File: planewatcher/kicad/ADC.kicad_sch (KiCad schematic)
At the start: 15 parts, among them U11 AD9203ARUZ

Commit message: update BoM to available parts from LCSC
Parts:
- RN2, RN3, RN4: MPN CAT16-22R0F4LF -> CAY16-22R0F4LF; lcsc_id C1731387 -> C1734385
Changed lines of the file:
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@@
 			)
 		)
-		(property "MPN" "CAT16-22R0F4LF"
+		(property "MPN" "CAY16-22R0F4LF"
 			(at 45.72 85.09 0)
 			(hide yes)
@@
 			)
 		)
-		(property "lcsc_id" "C1731387"
+		(property "lcsc_id" "C1734385"
 			(at 45.72 85.09 0)
 			(hide yes)
@@
 			)
 		)
-		(property "MPN" "CAT16-22R0F4LF"
+		(property "MPN" "CAY16-22R0F4LF"
 			(at 58.42 74.93 0)
 			(hide yes)
@@
 			)
 		)
-		(property "lcsc_id" "C1731387"
+		(property "lcsc_id" "C1734385"
 			(at 58.42 74.93 0)
 			(hide yes)
@@
 			)
 		)
-		(property "MPN" "CAT16-22R0F4LF"
+		(property "MPN" "CAY16-22R0F4LF"
 			(at 45.72 93.98 0)
 			(hide yes)
@@
 			)
 		)
-		(property "lcsc_id" "C1731387"
+		(property "lcsc_id" "C1734385"
 			(at 45.72 93.98 0)
 			(hide yes)

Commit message: Implement log detector output buffering & buffered low-pass filter for noise offset
- Implement low-pass filter to output noise floor with no pulses
- Feed noise floor into ADC driver -IN to improve range/sensitivity
- Buffer low pass filter output
- Buffer log detector output with spare op amp in OPA2320 package
- Tidy schematic & vias
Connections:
- net VREF: no longer names the net of C57.1, C58.1, TP21.1, U11.23 (VREF)
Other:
- moved on the sheet: TP21
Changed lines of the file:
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@@
+	)
+	(junction
+		(at 45.72 62.23)
+		(diameter 0)
+		(color 0 0 0 0)
 	)
 	(junction
@@
 	)
 	(junction
-		(at 45.72 62.23)
-		(diameter 0)
-		(color 0 0 0 0)
-	)
-	(junction
 		(at 59.69 62.23)
 		(diameter 0)
@@
 	)
 	(junction
-		(at 128.27 97.79)
-		(diameter 0)
-		(color 0 0 0 0)
-	)
-	(junction
 		(at 107.95 62.23)
 		(diameter 0)
@@
 		(pts
 			(xy 97.79 54.61) (xy 107.95 54.61)
-		)
-		(stroke
-			(width 0)
-			(type default)
-		)
-	)
-	(wire
-		(pts
-			(xy 128.27 97.79) (xy 135.89 97.79)
 		)
 		(stroke
@@
 	(wire
 		(pts
+			(xy 135.89 97.79) (xy 148.59 97.79)
+		)
+		(stroke
+			(width 0)
+			(type default)
+		)
+	)
+	(wire
+		(pts
 			(xy 64.77 90.17) (xy 69.85 90.17)
 		)
@@
 	(wire
 		(pts
-			(xy 121.92 97.79) (xy 128.27 97.79)
-		)
-		(stroke
-			(width 0)
-			(type default)
-		)
-	)
-	(wire
-		(pts
-			(xy 148.59 97.79) (xy 135.89 97.79)
+			(xy 121.92 97.79) (xy 135.89 97.79)
 		)
 		(stroke
@@
 		(shape input)
 		(at 97.79 66.04 0)
-		(effects
-			(font
-				(size 1.27 1.27)
-			)
-			(justify left)
-		)
-	)
-	(hierarchical_label "VREF"
-		(shape output)
-		(at 148.59 97.79 0)
 		(effects
 			(font
@@
 	(symbol
 		(lib_id "Connector:TestPoint")
-		(at 128.27 97.79 0)
+		(at 148.59 97.79 0)
+		(mirror x)
 		(unit 1)
 		(body_style 1)
@@
 		(in_pos_files yes)
 		(dnp no)
-		(fields_autoplaced yes)
 		(property "Reference" "TP21"
-			(at 130.81 93.2179 0)
+			(at 151.13 102.3621 0)
 			(show_name no)
 			(do_not_autoplace no)
@@
 		)
 		(property "Value" "VREF"
-			(at 130.81 95.7579 0)
+			(at 151.13 99.8221 0)
 			(show_name no)
 			(do_not_autoplace no)
@@
 		)
 		(property "Footprint" "TestPoint:TestPoint_Pad_D1.0mm"
-			(at 133.35 97.79 0)
+			(at 153.67 97.79 0)
 			(hide yes)
 			(show_name no)
@@
 		)
 		(property "Datasheet" ""
-			(at 133.35 97.79 0)
+			(at 153.67 97.79 0)
 			(hide yes)
 			(show_name no)
@@
 		)
 		(property "Description" "PCB copper test pad, 1.0mm, no fitted component"
-			(at 128.27 97.79 0)
+			(at 148.59 97.79 0)
 			(hide yes)
 			(show_name no)
@@
 		)
 		(property "Purpose" "Provides oscilloscope/DMM probe access to VREF."
-			(at 128.27 97.79 0)
-			(hide yes)
-			(show_name no)
+			(at 148.59 97.79 0)
+			(hide yes)
+			(show_name no)

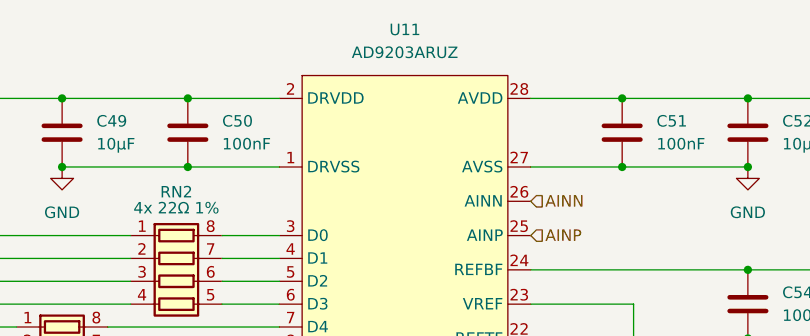
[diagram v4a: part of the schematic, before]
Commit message: Replace TADJ prototype trimmer with voltage divider
Voltage divider sets the ADL5513 TADJ pin to approximately 0.85 V for 1090 MHz operation
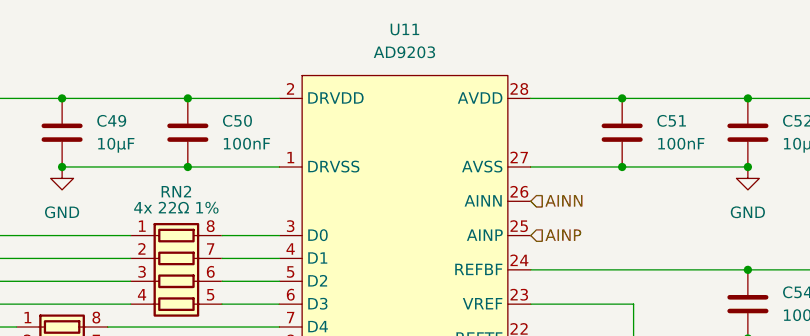
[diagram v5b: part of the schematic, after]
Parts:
- U11: value AD9203ARUZ -> AD9203
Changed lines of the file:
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@@
 			)
 		)
-		(property "Value" "AD9203ARUZ"
+		(property "Value" "AD9203"
 			(at 83.82 49.53 0)
 			(show_name no)

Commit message: Change all test point footprints to TestPoint_THTPad_D1.0mm_Drill0.5mm
Had to move TP15 slightly to prevent it shorting to 3V3.
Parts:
- TP21: footprint TestPoint:TestPoint_Pad_D1.0mm -> TestPoint:TestPoint_THTPad_D1.0mm_Drill0.5mm
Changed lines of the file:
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@@
 			)
 		)
-		(property "Footprint" "TestPoint:TestPoint_Pad_D1.0mm"
+		(property "Footprint" "TestPoint:TestPoint_THTPad_D1.0mm_Drill0.5mm"
 			(at 153.67 97.79 0)
 			(hide yes)
